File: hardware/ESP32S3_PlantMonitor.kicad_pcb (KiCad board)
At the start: 4 copper layers, 62.5 x 44.5 mm, 69 parts, among them J1 USB_C_Receptacle_USB2.0_16P, J2 Conn_01x03, J3 Conn_01x02, Q1 AO3401A, Q2 AO3401A, Q3 AO3401A, SW1 SW_Push, SW2 SW_Push, U1 USBLC6-2SC6, U2 AP2112K-3.3, U3 ESP32-S3-WROOM-1, U4 BME280, U5 VEML7700-TT, U6 MCP73831-2-OT

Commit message: Snapshot before final cleanup
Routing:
- net GND: vias 86 -> 88
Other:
- board text added: "Light Sensor (VEML7700)"
- board text removed: "LIGHT SENSOR"
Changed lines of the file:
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@@
+	)
+	(gr_rect
+		(start 30.725 54.25)
+		(end 50.5 67.25)
+		(stroke
+			(width 0.1)
+			(type default)
+		)
+		(fill no)
+		(layer "Cmts.User")
 	)
 	(gr_rect
 		(start 31 70.5)
 		(end 51.5 87.25)
-		(stroke
-			(width 0.1)
-			(type default)
-		)
-		(fill no)
-		(layer "Cmts.User")
-	)
-	(gr_rect
-		(start 38.25 54.25)
-		(end 50.5 67.25)
 		(stroke
 			(width 0.1)
@@
 	)
 	(gr_text "USB-C"
-		(at 34.5 70.5 0)
+		(at 28.375 70.5 0)
 		(layer "Cmts.User")
 		(effects
@@
 	)
 	(gr_text "LDO"
-		(at 42.75 54 0)
+		(at 30.325 54 0)
 		(layer "Cmts.User")
 		(effects
@@
 	)
 	(gr_text "soil sensor\n"
-		(at 72.5 77.4 0)
+		(at 71.875 97 0)
 		(layer "Cmts.User")
 		(effects
@@
 		)
 	)
-	(gr_text "LIGHT SENSOR"
+	(gr_text "Light Sensor (VEML7700)"
 		(at 98.5 80.7 0)
 		(layer "Cmts.User")
@@
 	)
 	(via
+		(at 82 60.475)
+		(size 0.6)
+		(drill 0.3)
+		(layers "F.Cu" "B.Cu")
+		(free yes)
+		(net "GND")
+	)
+	(via
 		(at 52.775 80.5)
 		(size 0.8)
@@
 		(size 0.6)
 		(drill 0.3)
+		(layers "F.Cu" "B.Cu")
+		(free yes)
+		(net "GND")
+	)
+	(via
+		(at 90.175 60.4)
+		(size 0.6)
+		(drill 0.3)

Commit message: DRC and ERC cleanup
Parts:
- moved R4 1.35 mm to (38.1, 84.5)
- moved U5 0.95 mm to (93.0, 81.5)
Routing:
- net GND: track 51.9 -> 72.6 mm, vias 88 -> 107
- net ADC_SOIL: track 45.4 -> 51.4 mm
- net Net-(J1-CC2): track 7.33 -> 8.95 mm
- net /02_USB_C_Input/USB_VBUS: track 27.8 -> 29.0 mm
- net +3V3: track 131.3 -> 130.4 mm
- net VBAT: track 77.4 -> 78.2 mm
- net +5V_PROT: track 78.8 -> 79.4 mm
- net SDA: track 35.1 -> 35.7 mm
- net Net-(D3-K): track 26.5 -> 27.1 mm
- net VSYS: track 23.2 -> 22.7 mm
- net Net-(J1-CC1): track 9.47 -> 8.97 mm

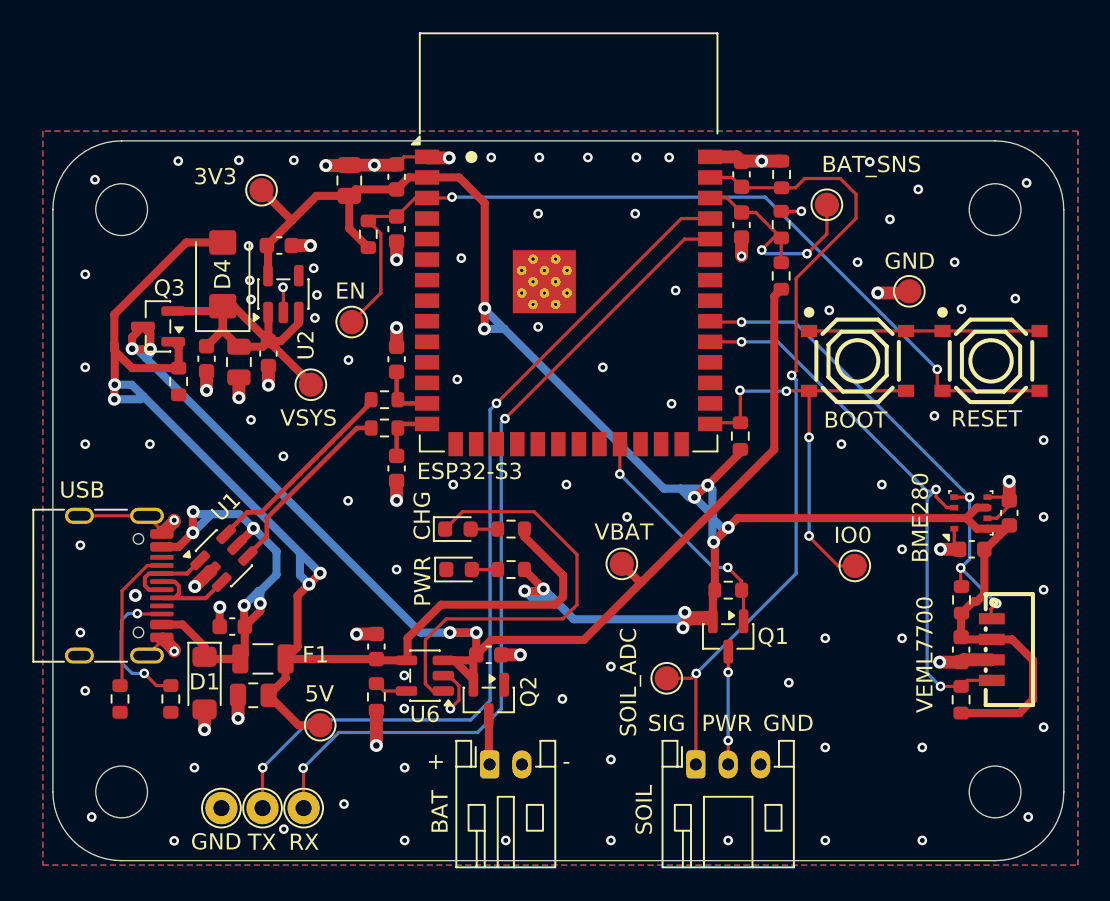
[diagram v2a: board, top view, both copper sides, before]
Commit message: Fab prep: board fixes, documentation refresh, order notes, license
Board/schematic:
- USB-C ground pads to solid zone connection with adjacent stitching vias
- C3/C4 DNP + BOM/CPL exclusion flags synced between schematic and board
- Silkscreen text cleanup

Docs & repo:
- PROJECT_STATUS and guides updated to as-built pre-order state
- JLCPCB order notes added (fabrication/revA): settings, panel remark, stock check
- CERN-OHL-P v2 license; board renders in README
- JLC plugin cache untracked; standards texts referenced outside the repo
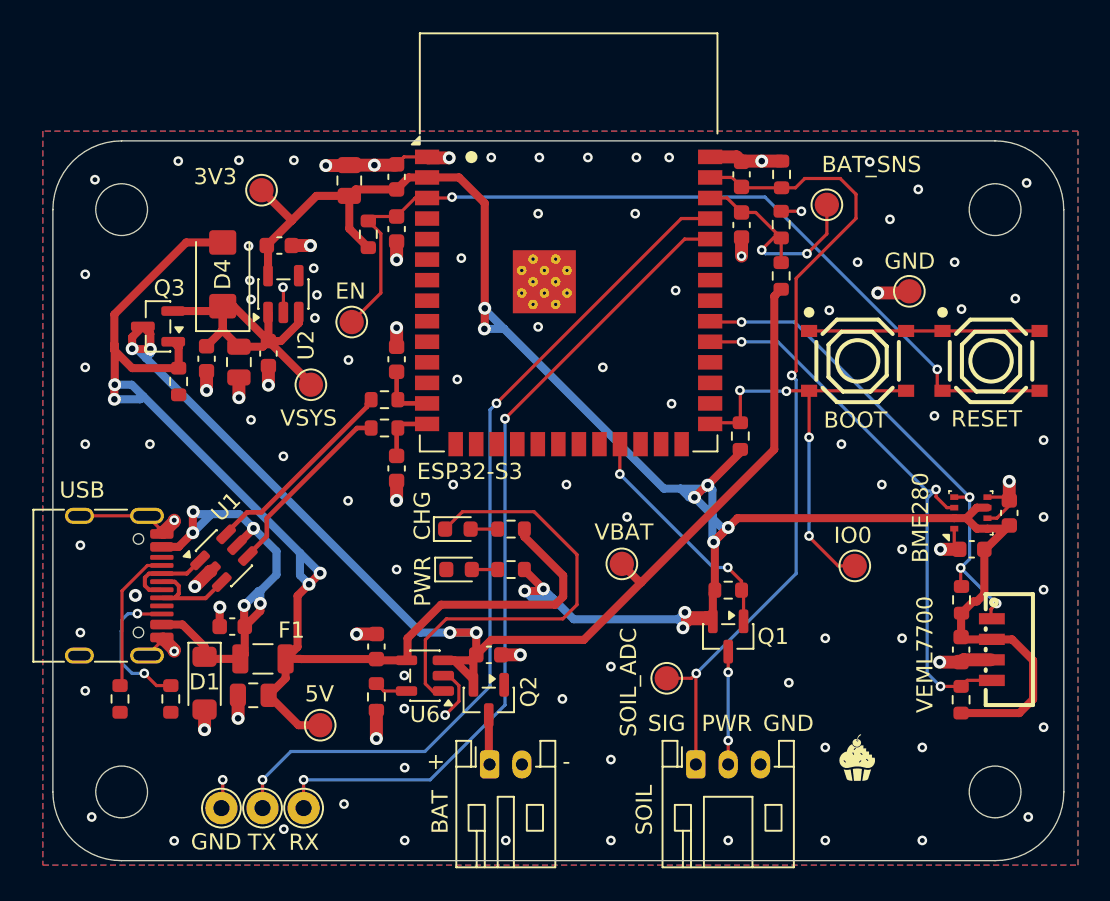
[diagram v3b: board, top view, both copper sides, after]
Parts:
- added G***: LOGO, logos:muffinByteLogo, F.Cu at (83.7, 88.4)
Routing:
- net GND: track 72.6 -> 74.5 mm
- net /04_ESP32S3_Core/TXD0: track 54.8 -> 53.8 mm

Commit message: pre-order baseline
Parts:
- removed G***: LOGO, logos:muffinByteLogo
- added G1: muffinByteLogo_2x, logos:muffinByteLogo_2x, F.Cu at (84.8, 90.2)
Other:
- board text added: "ESP32-S3 PLANT MONITOR - REV A - FABRICATION AND ASSEMBLY NOTES MuffinByteLabs - Ray Malik - 2026-08 FABRICATION 1. Material FR-4, 4 layers, finished thickness 1.6 mm. 2. Stackup: JLCPCB JLC04161H-7628. L1 F.Cu - 1.0 oz - signal L2 In1.Cu - 0.5 oz - GND plane L3 In2.Cu - 0.5 oz - GND plane L4 B.Cu - 1.0 oz - signal 3. Surface finish: HASL lead-free. Solder mask green both sides, silkscreen white 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"
- board text added: "ESP32-S3 PLANT MONITOR Rev A 2026-08 MuffinByteLabs.com Designed by Ray Malik"
- board text added: "JLCJLCJLCJLC"
